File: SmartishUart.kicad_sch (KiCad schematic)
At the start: 29 parts, among them J1 USB_C_Receptacle_USB2.0, J2 UART, J3 V_SEL, J4 Conn_01x07, J5 PROG_SEL, J6 RESET_SEL, Q1 MMBT2222, Q2 MMBT2222, SW1 TL3342, SW2 TL3342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

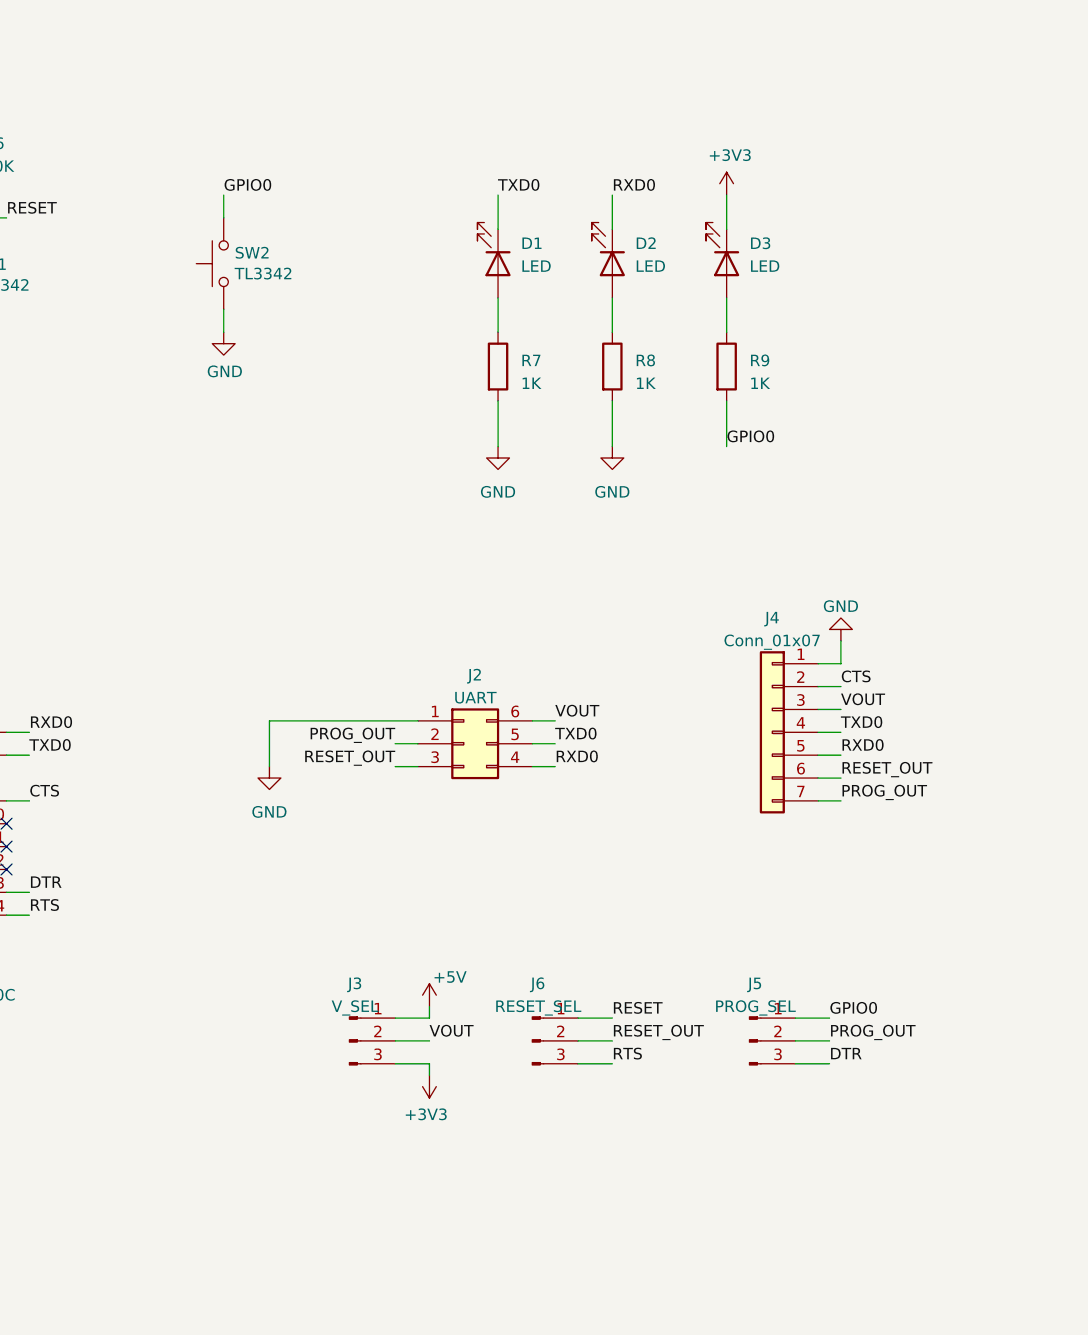
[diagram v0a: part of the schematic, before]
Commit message: Various updates
- Added LED to all output pins
- Dropped pogopin area
- Made 'CTS' pin configurable
- Added lots of lables
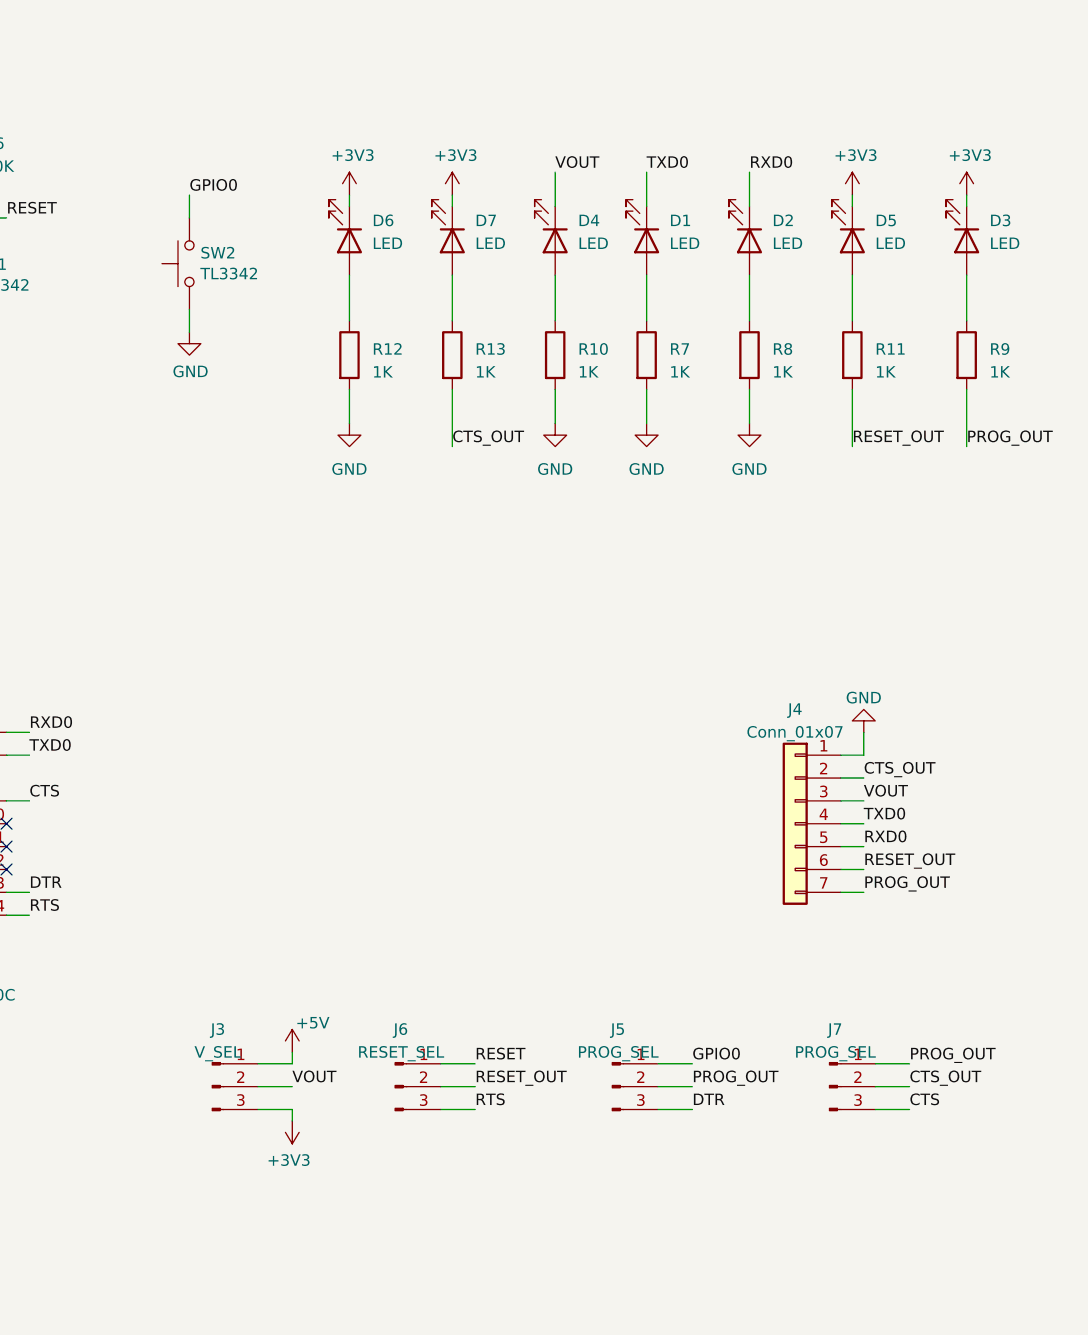
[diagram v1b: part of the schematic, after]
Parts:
- removed J2: UART, SmartishUart:Prog_1, symbol Connector_Generic:Conn_02x03_Counter_Clockwise
- added D4, D5, D6, D7: LED, LED_SMD:LED_0805_2012Metric, symbol Device:LED
- added J7: PROG_SEL, Connector_PinHeader_2.54mm:PinHeader_1x03_P2.54mm_Vertical, symbol Connector:Conn_01x03_Pin
- added R10, R11, R12, R13: 1K, Resistor_SMD:R_0805_2012Metric, symbol Device:R
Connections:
- net +3V3: now also D5.1 (K), D6.1 (K), D7.1 (K)
- net CTS: now also J7.3 (Pin_3); no longer J4.2 (Pin_2)
- net GND: now also R10.2, R12.2
- net GPIO0: no longer R9.2
- net PROG_OUT: now also R9.2, J7.1 (Pin_1)
- net RESET_OUT: now also R11.2
- net VOUT: now also D4.1 (K)
- new net: D5.2 (A), R11.1
- new net: D4.2 (A), R10.1
- new net: D6.2 (A), R12.1
- new net: D7.2 (A), R13.1
- new net CTS_OUT: J4.2 (Pin_2), J7.2 (Pin_2), R13.2
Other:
- moved on the sheet: D1, D2, D3, J3, J4, J5, J6, R7, R8, R9, SW2
